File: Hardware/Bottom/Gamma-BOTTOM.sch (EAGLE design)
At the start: 32 parts, among them U1 AD5242-SO16

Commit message: Finished Bottom Board as of Take 003
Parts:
- removed J1: (no value), LinnesLab-Connectors:CONN_07
- added C2: 100n, LinnesLab-Passives:CAPACITOR0603
- added J2: (no value), LinnesLab-Connectors:CONN_07-1.27MM
- renumbered OP4 to TIA, U$4 to AD5171, U1 to AD5242
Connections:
- removed net LED: Q1.C
- net 3.3V: now also J2.4
- net A6/TIA: now also J2.6; no longer J1.5
- net A7/PPG: now also J2.7; no longer J1.7
- net D29/LED.CTRL: now also J2.5; no longer J1.6
- net GND: now also C2.1, J2.3
- net LED.C: now also Q1.C
- net SCL: now also J2.2
- net SDA: now also J2.1
- net VREF: now also C2.2
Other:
- note added: "Gamma Bottom Board - Version A"
- note added: "Pins"
- moved on the sheet: C1, IMU1

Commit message: Pushed Changes to where I'm at (Take 007)
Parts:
- added C12, C3, C5: 1u, LinnesLab-Passives:CAPACITOR0603
- added C13, C4: 4.7u, LinnesLab-Passives:CAPACITOR0603
- added CHRG1: MCP73831, LinnesLab-Power:MCP73831
- added LDO1: MIC5504, LinnesLab-Power:MIC5504
- added R3: 100k, LinnesLab-Passives:RESISTOR0603
- added R8: (no value), LinnesLab-Passives:RESISTOR0603
- added U4: PCF8523, LinnesLab-Clocks:PCF8523
- added XTAL2: 32.7680kHz, LinnesLab-Clocks:CRYSTALECS-.327-12.5-12-C-TR
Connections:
- new net D27/CHRG.STATUS: CHRG1.STAT, R3.1
- new net N$1: U4.OSCO, XTAL2.1
- new net N$2: U4.OSCI, XTAL2.2
- new net N$3: CHRG1.PROG, R8.2
- new net VBATT: U4.VBAT
- new net VIN1: C4.2, C5.2, CHRG1.VIN, LDO1.EN, LDO1.IN, R3.2
- new net VLIPO: C13.1, CHRG1.VBAT
- net 3.3V: now also C12.1, C3.1, LDO1.OUT, U4.VDD
- net GND: now also C12.2, C13.2, C3.2, C4.1, C5.1, CHRG1.VSS, LDO1.GND, R8.1, U4.VSS
- net SCL: now also U4.SCL
- net SDA: now also U4.SDA
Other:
- note added: "Back-up battery if desired"
- note added: "Bottom Board Power Management"
- note added: "I2C Address = 0x68h"
- note added: "Real-Time Clock"

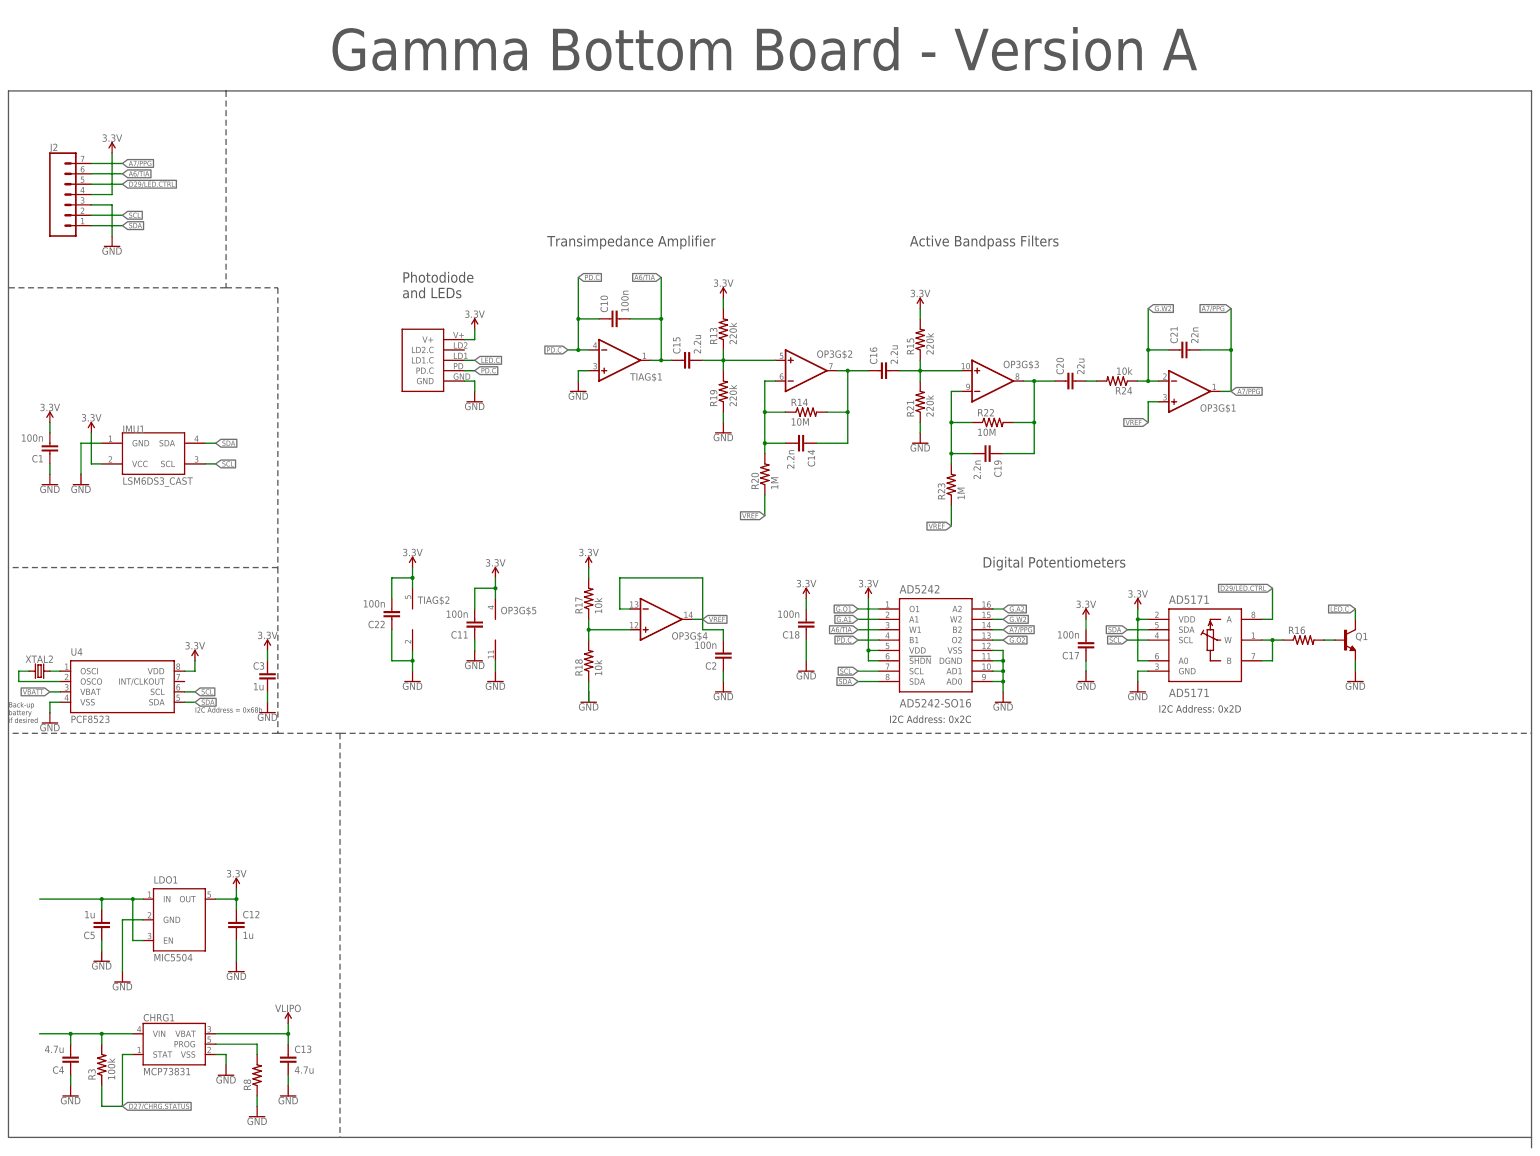
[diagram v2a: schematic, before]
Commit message: Finished with Preliminary Version A of Smartwatch as of end of Take 008 video
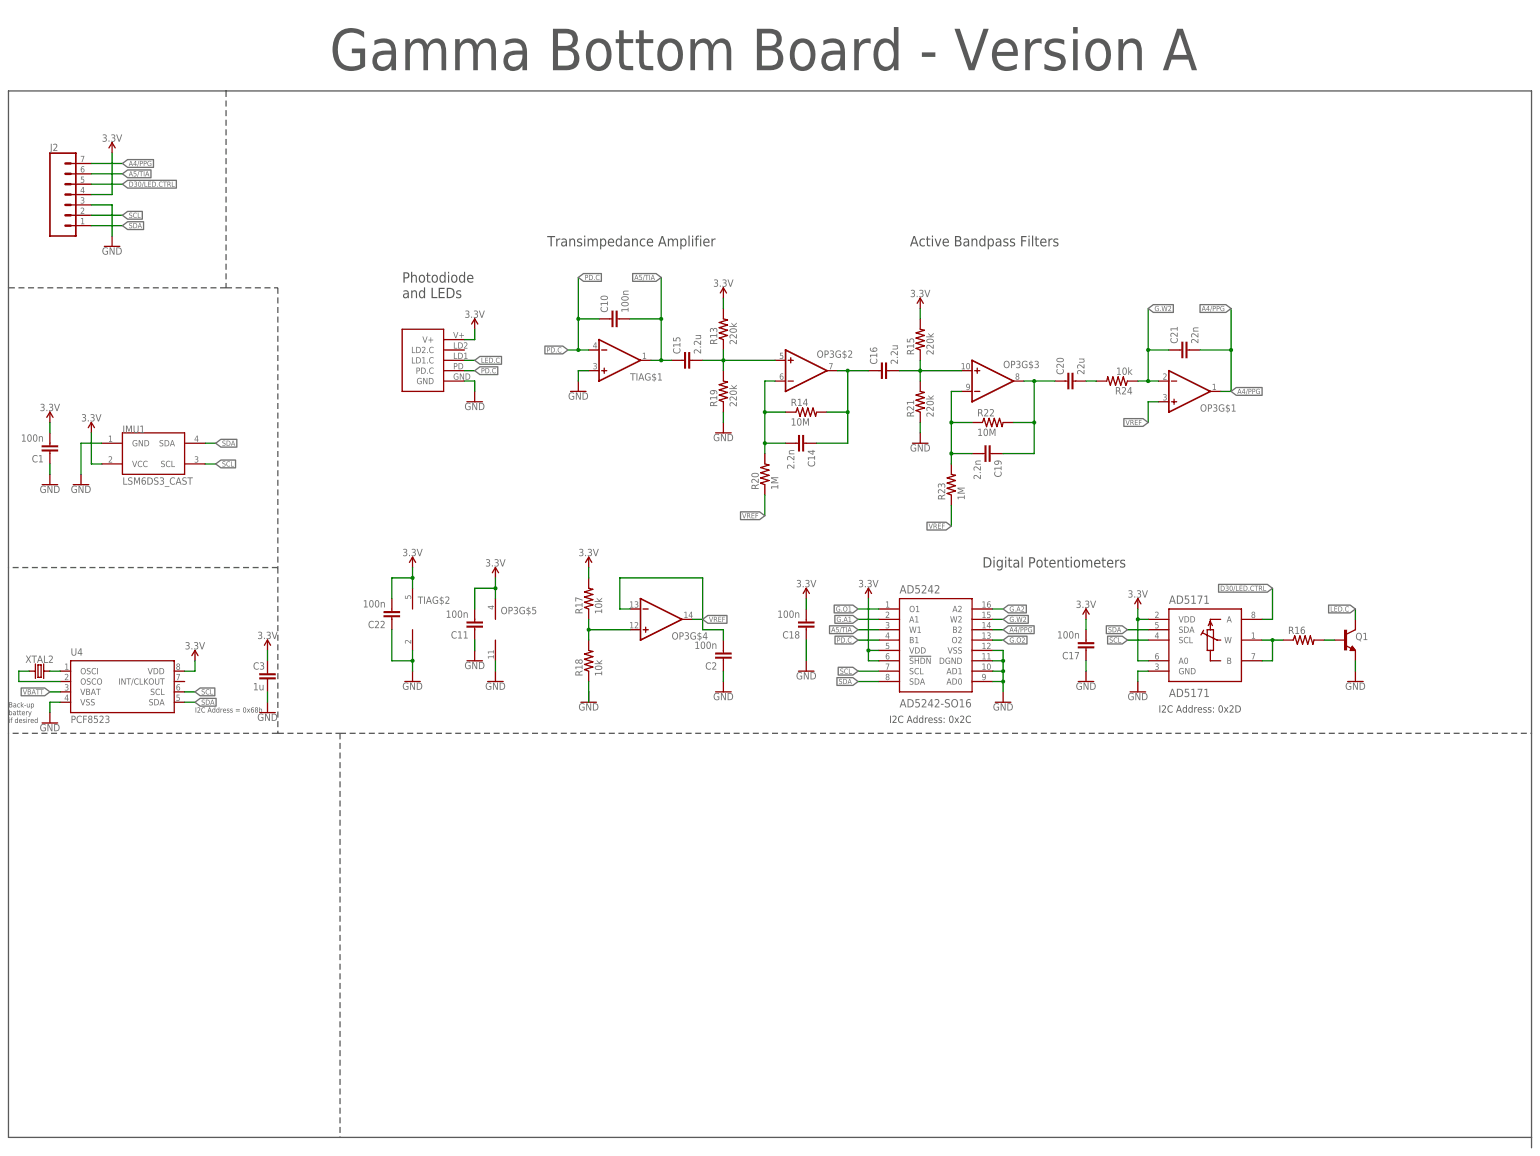
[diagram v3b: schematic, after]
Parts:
- removed C12, C5: 1u, LinnesLab-Passives:CAPACITOR0603
- removed C13, C4: 4.7u, LinnesLab-Passives:CAPACITOR0603
- removed CHRG1: MCP73831, LinnesLab-Power:MCP73831
- removed LDO1: MIC5504, LinnesLab-Power:MIC5504
- removed R3: 100k, LinnesLab-Passives:RESISTOR0603
- removed R8: (no value), LinnesLab-Passives:RESISTOR0603
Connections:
- net A6/TIA renamed A5/TIA
- net A7/PPG renamed A4/PPG
- net D29/LED.CTRL renamed D30/LED.CTRL
- removed net D27/CHRG.STATUS: CHRG1.STAT, R3.1
- removed net N$3: CHRG1.PROG, R8.2
- removed net VIN1: C4.2, C5.2, CHRG1.VIN, LDO1.EN, LDO1.IN, R3.2
- removed net VLIPO: C13.1, CHRG1.VBAT
- net 3.3V: no longer C12.1, LDO1.OUT
- net GND: no longer C12.2, C13.2, C4.1, C5.1, CHRG1.VSS, LDO1.GND, R8.1
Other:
- note removed: "Bottom Board Power Management"
